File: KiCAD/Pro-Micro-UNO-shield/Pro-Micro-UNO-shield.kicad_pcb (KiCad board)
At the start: 2 copper layers, 68.6 x 53 mm, 58 parts, among them J1 Arduino_pro_micro, J15 Debug LED enable, J2 Arduino UNO, J3 Conn_01x10_Male, J5 Arduino_pro_micro WIDE, J6 Conn_01x10_Male, J7 Conn_01x02_Male

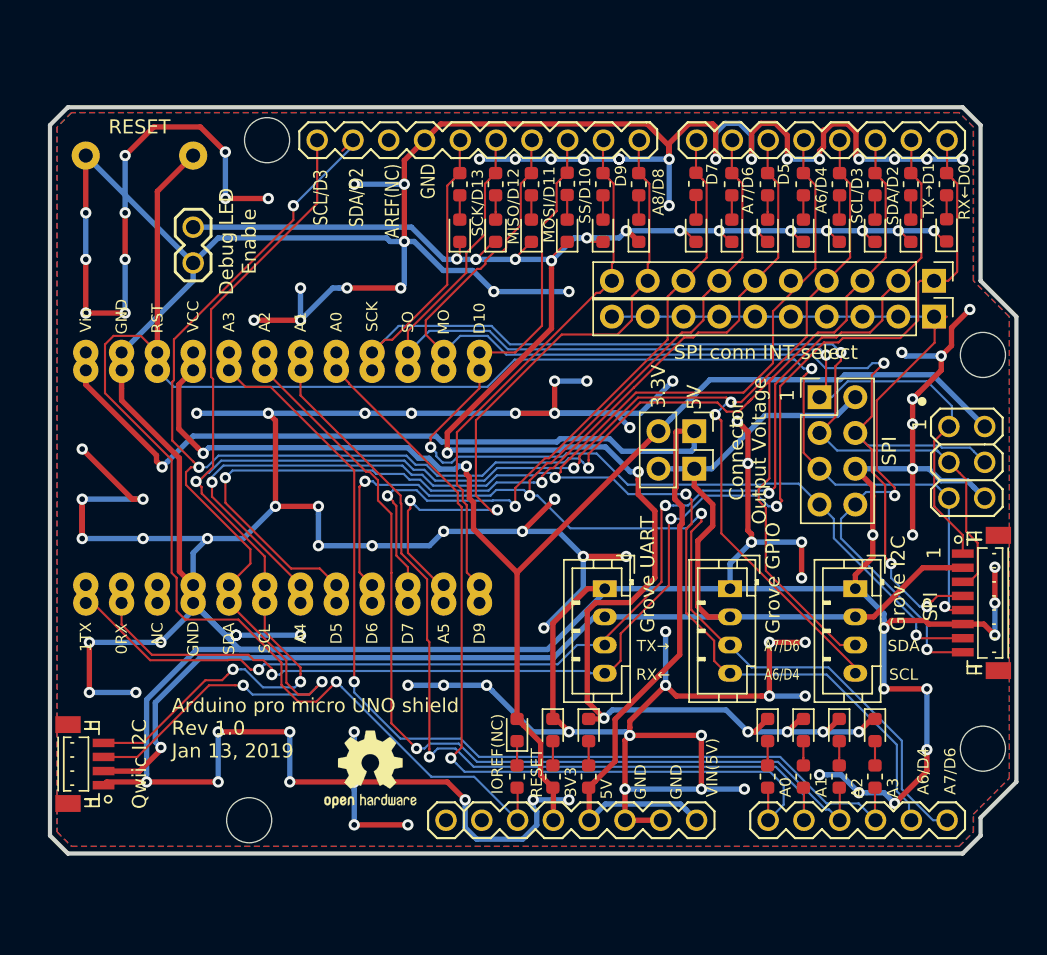
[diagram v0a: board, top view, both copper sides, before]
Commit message: Pro micro UNO shield Rev1.1 (Fixed Qwiic connector pin assign)
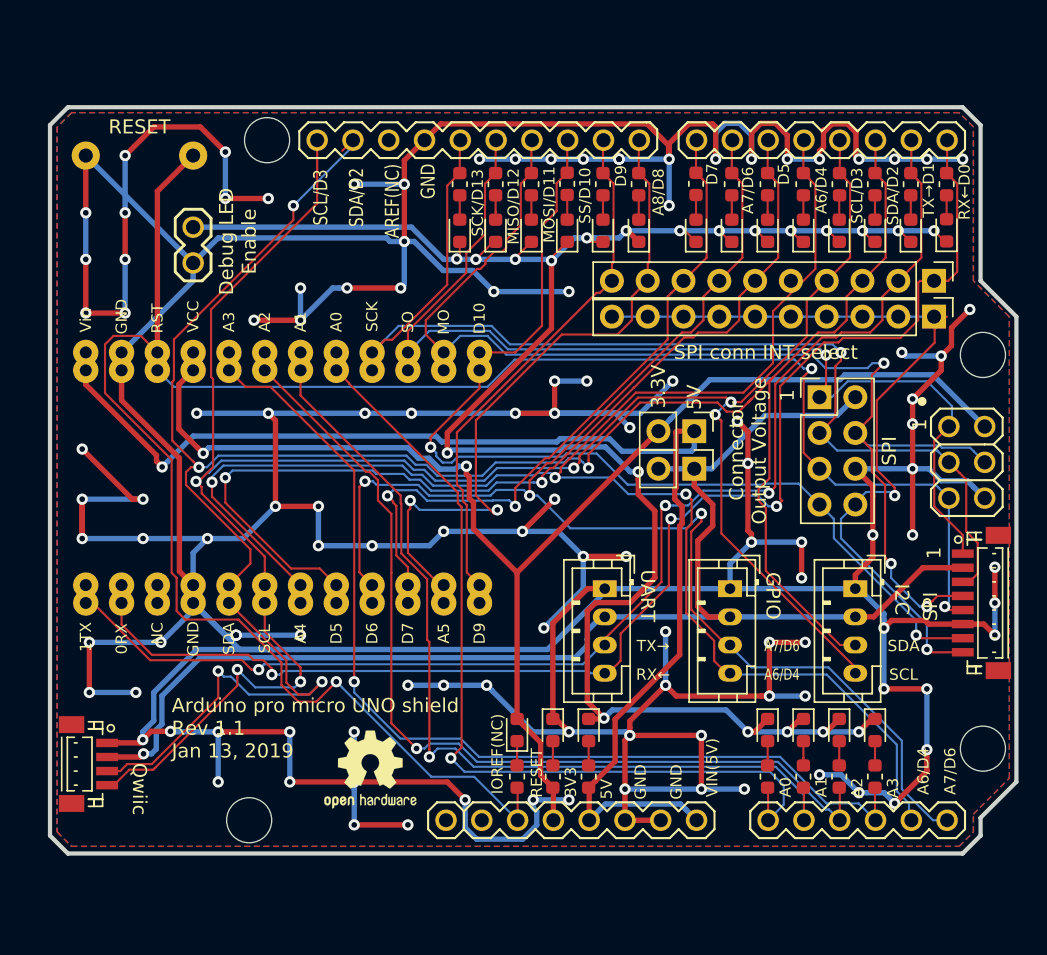
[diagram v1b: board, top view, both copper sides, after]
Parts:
- removed the Qwiic I2C at (123.2, 160.0)
- added Qwiic I2C: Qwiic I2c, library:Qwiic_I2C_1.00mm_4pin, F.Cu at (123.4, 160.0)
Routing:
- net GND: track 664.8 -> 661.9 mm, vias 119 -> 120
- net SDA: track 162.7 -> 164.9 mm
- net SCL: track 150.9 -> 152.7 mm
- net VCC-CONN: track 98.9 -> 98.3 mm
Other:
- board text added: "Arduino pro micro UNO shield Rev 1.1 Jan 13, 2019"
- board text added: "GPIO"
- board text added: "I2C"
- board text added: "Qwiic"
- board text added: "UART"
- board text removed: "Arduino pro micro UNO shield Rev 1.0 Jan 13, 2019"

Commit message: Pro Micro UNO shield v2.0 (Diag shield)
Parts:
- removed Connector output Voltage: Conn_01x02_Male, KiCAD footprints:PinHeader_1x02_P2.54mm_Vertical
- removed Grove GPIO: Grove GPIO, library:JST_PH_B4B-PH-K_04x2.00mm_Straight
- removed Grove I2C: Grove I2C, library:JST_PH_B4B-PH-K_04x2.00mm_Straight
- removed Grove UART: Grove UART, library:JST_PH_B4B-PH-K_04x2.00mm_Straight
- removed J15: Debug LED enable, freetronics_footprints:1X02
- removed the J2 at (120.8, 166.5)
- removed Qwiic I2C: Qwiic I2c, library:Qwiic_I2C_1.00mm_4pin
- removed RESET: Reset switch, library:push switch
- removed SPI: SPI header, KiCAD footprints:PinHeader_2x04_P2.54mm_Vertical
- removed SPI: SPI connector, library:JST_SH_BM08B-SRSS-TB_08x1.00mm_Straight
- added D22: BLUE, LED_SMD:LED_0603_1608Metric, F.Cu at (156.0, 110.0)
- added D23: BLUE, LED_SMD:LED_0603_1608Metric, F.Cu at (158.5, 110.0)
- added D24: BLUE, LED_SMD:LED_0603_1608Metric, F.Cu at (161.0, 110.0)
- added D25: PWR, LED_SMD:LED_0603_1608Metric, F.Cu at (154.9, 166.6)
- added D26: RED, LED_SMD:LED_0603_1608Metric, F.Cu at (182.9, 166.7)
- added D27: RED, LED_SMD:LED_0603_1608Metric, F.Cu at (180.4, 166.7)
- added D28: RED, LED_SMD:LED_0603_1608Metric, F.Cu at (177.8, 166.7)
- added D29: RED, LED_SMD:LED_0603_1608Metric, F.Cu at (175.3, 166.7)
- added D30: RED, LED_SMD:LED_0603_1608Metric, F.Cu at (172.8, 166.7)
- added D31: RED, LED_SMD:LED_0603_1608Metric, F.Cu at (170.2, 166.7)
- added D32: RED, LED_SMD:LED_0603_1608Metric, F.Cu at (152.4, 166.7)
- added D33: RED, LED_SMD:LED_0603_1608Metric, F.Cu at (149.9, 166.8)
- added D34: RED, LED_SMD:LED_0603_1608Metric, F.Cu at (165.1, 112.8)
- added D35: RED, LED_SMD:LED_0603_1608Metric, F.Cu at (167.6, 112.8)
- added D36: RED, LED_SMD:LED_0603_1608Metric, F.Cu at (170.2, 112.8)
- added D37: RED, LED_SMD:LED_0603_1608Metric, F.Cu at (172.7, 112.8)
- added D38: RED, LED_SMD:LED_0603_1608Metric, F.Cu at (175.3, 112.8)
- added D39: RED, LED_SMD:LED_0603_1608Metric, F.Cu at (177.8, 112.8)
- added D40: RED, LED_SMD:LED_0603_1608Metric, F.Cu at (180.3, 112.8)
- added D41: RED, LED_SMD:LED_0603_1608Metric, F.Cu at (182.9, 112.8)
- added D42: RED, LED_SMD:LED_0603_1608Metric, F.Cu at (138.2, 112.8)
- added D43: RED, LED_SMD:LED_0603_1608Metric, F.Cu at (140.7, 112.8)
- added D44: RED, LED_SMD:LED_0603_1608Metric, F.Cu at (148.3, 112.8)
- added D45: RED, LED_SMD:LED_0603_1608Metric, F.Cu at (150.9, 112.8)
- added D46: RED, LED_SMD:LED_0603_1608Metric, F.Cu at (153.4, 112.8)
- added D47: RED, LED_SMD:LED_0603_1608Metric, F.Cu at (156.0, 112.8)
- added D48: RED, LED_SMD:LED_0603_1608Metric, F.Cu at (158.5, 112.8)
- added D49: RED, LED_SMD:LED_0603_1608Metric, F.Cu at (161.0, 112.8)
- added D50: PWR, LED_SMD:LED_0603_1608Metric, F.Cu at (157.5, 166.6)
- added J10: Grove UART, library:JST_PH_B4B-PH-K_04x2.00mm_Straight, F.Cu at (158.8, 147.6)
- added J11: Grove GPIO, library:JST_PH_B4B-PH-K_04x2.00mm_Straight, F.Cu at (167.6, 147.6)
- added J12: SPI header, Connector_PinSocket_2.54mm:PinSocket_2x04_P2.54mm_Vertical, B.Cu at (173.9, 133.9)
- added J13: SPI connector, library:JST_SH_BM08B-SRSS-TB_08x1.00mm_Straight, F.Cu at (185.2, 148.6)
- added J2 (x2): Arduino UNO, library:Arduino_Shield, F.Cu at (119.4, 166.4)
- added J4: Conn_01x02_Male, Connector_PinSocket_2.54mm:PinSocket_1x02_P2.54mm_Vertical, F.Cu at (165.0, 136.3)
- added J8: Grove I2C, library:JST_PH_B4B-PH-K_04x2.00mm_Straight, F.Cu at (176.5, 147.6)
- added J9: Qwiic I2c, library:Qwiic_I2C_1.00mm_4pin, F.Cu at (122.2, 160.0)
- added R22: 220R, Resistor_SMD:R_0603_1608Metric, B.Cu at (156.0, 110.0)
- added R23: 220R, Resistor_SMD:R_0603_1608Metric, B.Cu at (158.5, 110.0)
- added R24: 220R, Resistor_SMD:R_0603_1608Metric, B.Cu at (161.0, 110.0)
- added R25: 220R, Resistor_SMD:R_0603_1608Metric, F.Cu at (154.9, 169.4)
- added R26: 220R, Resistor_SMD:R_0603_1608Metric, B.Cu at (182.9, 166.7)
- added R27: 220R, Resistor_SMD:R_0603_1608Metric, B.Cu at (180.4, 166.7)
- added R28: 220R, Resistor_SMD:R_0603_1608Metric, B.Cu at (177.8, 166.7)
- added R29: 220R, Resistor_SMD:R_0603_1608Metric, B.Cu at (175.3, 166.7)
- added R30: 220R, Resistor_SMD:R_0603_1608Metric, B.Cu at (172.8, 166.7)
- added R31: 220R, Resistor_SMD:R_0603_1608Metric, B.Cu at (170.2, 166.7)
- added R32: 220R, Resistor_SMD:R_0603_1608Metric, B.Cu at (152.4, 166.7)
- added R33: 220R, Resistor_SMD:R_0603_1608Metric, B.Cu at (149.9, 166.8)
- added R34: 220R, Resistor_SMD:R_0603_1608Metric, B.Cu at (165.1, 112.8)
- added R35: 220R, Resistor_SMD:R_0603_1608Metric, B.Cu at (167.6, 112.8)
- added R36: 220R, Resistor_SMD:R_0603_1608Metric, B.Cu at (170.2, 112.8)
- added R37: 220R, Resistor_SMD:R_0603_1608Metric, B.Cu at (172.7, 112.8)
- added R38: 220R, Resistor_SMD:R_0603_1608Metric, B.Cu at (175.3, 112.8)
- added R39: 220R, Resistor_SMD:R_0603_1608Metric, B.Cu at (177.8, 112.8)
- added R40: 220R, Resistor_SMD:R_0603_1608Metric, B.Cu at (180.3, 112.8)
- added R41: 220R, Resistor_SMD:R_0603_1608Metric, B.Cu at (182.9, 112.8)
- added R42: 220R, Resistor_SMD:R_0603_1608Metric, B.Cu at (138.2, 112.8)
- added R43: 220R, Resistor_SMD:R_0603_1608Metric, B.Cu at (140.7, 112.8)
- added R44: 220R, Resistor_SMD:R_0603_1608Metric, B.Cu at (148.3, 112.8)
- added R45: 220R, Resistor_SMD:R_0603_1608Metric, B.Cu at (150.9, 112.8)
- added R46: 220R, Resistor_SMD:R_0603_1608Metric, B.Cu at (153.4, 112.8)
- added R47: 220R, Resistor_SMD:R_0603_1608Metric, B.Cu at (156.0, 112.8)
- added R48: 220R, Resistor_SMD:R_0603_1608Metric, B.Cu at (158.5, 112.8)
- added R49: 220R, Resistor_SMD:R_0603_1608Metric, B.Cu at (161.0, 112.8)
- added R50: 220R, Resistor_SMD:R_0603_1608Metric, F.Cu at (157.5, 169.4)
- added SW1: Reset switch, library:push switch, F.Cu at (126.4, 111.1)
- added SW2: SW_SPDT, library:mini_slide_switch, F.Cu at (125.7, 121.9)
- added U1: SN74LVC541ADBR, library:SN74LVC541ADBR, F.Cu at (150.0, 157.9)
- added U2: SN74LVC541ADBR, library:SN74LVC541ADBR, F.Cu at (150.7, 121.8)
- added U3: SN74LVC541ADBR, library:SN74LVC541ADBR, F.Cu at (136.5, 123.6)
- D1, D10, D11, D12, D13, D14, D15, D16, D17, D18, D19, D2, D20, D21, D3, D4, D5, D6, D7, D8, D9: value LED -> BLUE
- R1, R10, R11, R12, R13, R14, R15, R16, R17, R18, R19, R2, R20, R21, R3, R4, R5, R6, R7, R8, R9: value R 1K -> 220R; moved to B.Cu
- moved R17 63.8 mm to (138.2, 110.0)
- moved R18 63.8 mm to (140.7, 110.0)
- moved D17 61.2 mm to (138.2, 110.0), turned to 90 degrees
- moved D18 61.2 mm to (140.7, 110.0), turned to 90 degrees
- moved R8 58.6 mm to (149.9, 169.5)
- moved R7 56.1 mm to (152.4, 169.5)
- moved D8 55.7 mm to (149.9, 169.5), turned to 270 degrees
- moved R1 55.6 mm to (182.9, 169.5)
- moved R2 53.7 mm to (180.4, 169.5)
- moved D7 53.2 mm to (152.4, 169.5), turned to 270 degrees
- moved D1 52.6 mm to (182.9, 169.5), turned to 270 degrees
- moved R19 52.0 mm to (148.3, 110.0)
- moved R3 51.9 mm to (177.8, 169.5)
- moved R15 51.7 mm to (180.3, 110.0)
- moved R16 51.7 mm to (182.9, 110.0)
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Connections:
- D10 pad 1: Net-(D1-Pad1) -> Net-(D10-Pad1)
- D11 pad 1: Net-(D1-Pad1) -> Net-(D11-Pad1)
- D12 pad 1: Net-(D1-Pad1) -> Net-(D12-Pad1)
- D13 pad 1: Net-(D1-Pad1) -> Net-(D13-Pad1)
- D14 pad 1: Net-(D1-Pad1) -> Net-(D14-Pad1)
- D15 pad 1: Net-(D1-Pad1) -> Net-(D15-Pad1)
- D16 pad 1: Net-(D1-Pad1) -> Net-(D16-Pad1)
- D17 pad 1: Net-(D1-Pad1) -> Net-(D17-Pad1)
- D18 pad 1: Net-(D1-Pad1) -> Net-(D18-Pad1)
- D19 pad 1: Net-(D1-Pad1) -> Net-(D19-Pad1)
- D2 pad 1: Net-(D1-Pad1) -> Net-(D2-Pad1)
- D20 pad 1: GND -> Net-(D20-Pad1)
- D21 pad 2: 3.3V -> Net-(D21-Pad2)
- D3 pad 1: Net-(D1-Pad1) -> Net-(D28-Pad2)
- D4 pad 1: Net-(D1-Pad1) -> Net-(D29-Pad2)
- D5 pad 1: Net-(D1-Pad1) -> Net-(D30-Pad2)
- D6 pad 1: Net-(D1-Pad1) -> Net-(D31-Pad2)
- D7 pad 1: Net-(D1-Pad1) -> Net-(D32-Pad2)
- D8 pad 1: Net-(D1-Pad1) -> Net-(D33-Pad2)
- D9 pad 1: Net-(D1-Pad1) -> Net-(D34-Pad2)
- R1 pad 2: D9 -> 3.3V
- R10 pad 2: TX -> 3.3V
- R11 pad 2: D10/SS -> 3.3V
- R12 pad 2: MOSI -> 3.3V
- R13 pad 2: MISO -> 3.3V
- R14 pad 2: SCK -> 3.3V
- R15 pad 2: A0 -> 3.3V
- R16 pad 2: A1 -> 3.3V
- R17 pad 2: A2 -> 3.3V
- R18 pad 2: A3 -> 3.3V
- R19 pad 2: 5V -> 3.3V
- R2 pad 2: D8/A8 -> 3.3V
- R21 pad 1: Net-(D21-Pad1) -> Net-(D21-Pad2)
- R21 pad 2: RESET -> 3.3V
- R3 pad 2: D7 -> 3.3V
- R4 pad 2: D6/A7 -> 3.3V
- R5 pad 2: D5 -> 3.3V
- R6 pad 2: D4/A6 -> 3.3V
- R7 pad 2: SCL -> 3.3V
- R8 pad 2: SDA -> 3.3V
- R9 pad 2: RX -> 3.3V
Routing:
- net GND: track 661.9 -> 379.6 mm, vias 120 -> 202
- net 3.3V: track 96.1 -> 241.9 mm, vias 2 -> 9
- net /debug_led/OE: track 0.00 -> 128.4 mm, vias 0 -> 8
- net Net-(D1-Pad1): track 153.1 -> 37.7 mm, vias 21 -> 2
- net TX: track 91.9 -> 147.0 mm, vias 3 -> 8
- net RX: track 96.4 -> 147.6 mm, vias 3 -> 8
- net Net-(D23-Pad1): track 0.00 -> 47.1 mm, vias 0 -> 2
- net Net-(D24-Pad1): track 0.00 -> 42.5 mm, vias 0 -> 2
- net Net-(D16-Pad1): track 0.00 -> 41.5 mm, vias 0 -> 2
- net Net-(D15-Pad1): track 0.00 -> 37.5 mm, vias 0 -> 2
- net Net-(D2-Pad1): track 0.00 -> 36.1 mm, vias 0 -> 2
- net Net-(D14-Pad1): track 0.00 -> 34.8 mm, vias 0 -> 2
- net Net-(D28-Pad2): track 0.00 -> 33.8 mm, vias 0 -> 2
- net Net-(D22-Pad1): track 0.00 -> 33.4 mm, vias 0 -> 2
- net Net-(D13-Pad1): track 0.00 -> 32.5 mm, vias 0 -> 2
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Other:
- board size 68.6 x 53 mm -> 68.6 x 63.5 mm
- board text added: "Arduino pro micro Diag shield Rev 2.0 Mar 3, 2019"
- board text added: "Debug LED"
- board text added: "GND"
- board text added: "INT"
- board text added: "MISO"
- board text added: "MOSI"
- board text added: "RESET"
- board text added: "RST"
- board text added: "SCK"
- board text added: "SS"
- board text added: "VCC"
- board text removed: "Arduino pro micro UNO shield Rev 1.1 Jan 13, 2019"
- board text removed: "Debug LED Enable"
